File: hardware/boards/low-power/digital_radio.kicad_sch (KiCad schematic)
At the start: 34 parts, among them J1 U.FL, U1 SX1262IMLTRT, U2 SKY13453-385LF, Y1 32 MHz

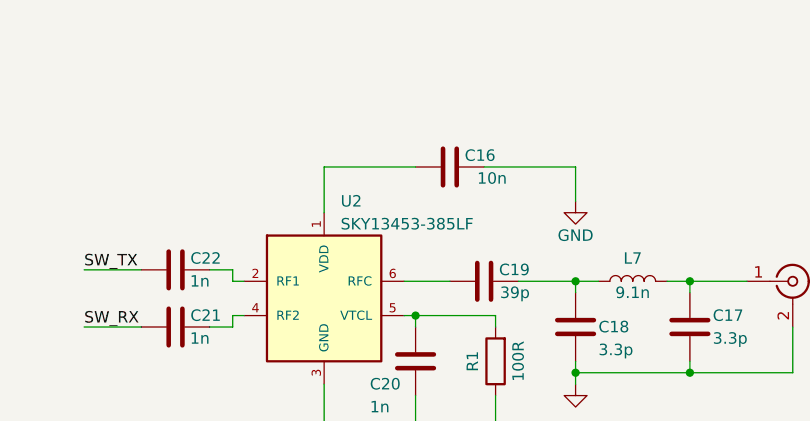
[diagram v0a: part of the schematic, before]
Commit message: fixup! Add low power PCB
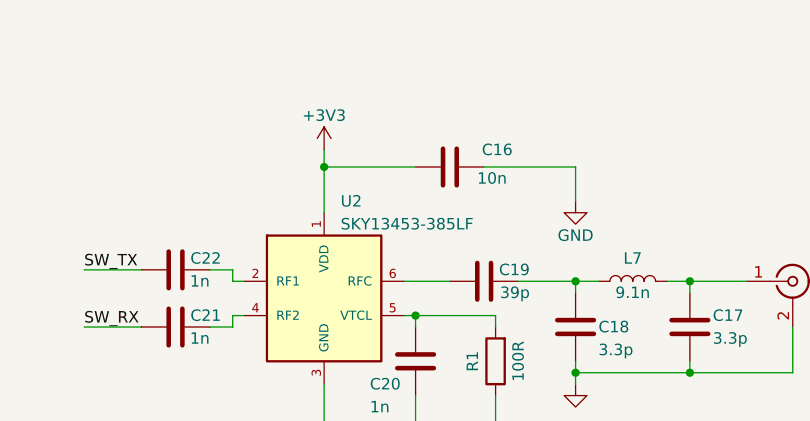
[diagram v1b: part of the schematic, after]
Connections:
- net +3V3: now also C16.1, U2.1 (VDD)
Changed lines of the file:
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@@
   (junction (at 112.395 102.235) (diameter 0) (color 0 0 0 0)
+  )
+  (junction (at 219.71 66.675) (diameter 0) (color 0 0 0 0)
   )
   (junction (at 139.065 79.375) (diameter 0) (color 0 0 0 0)
@@
   (no_connect (at 60.325 99.695))
   (wire (pts (xy 76.835 109.855) (xy 76.835 112.395))
+    (stroke (width 0) (type default))
+  )
+  (wire (pts (xy 219.71 64.77) (xy 219.71 66.675))
     (stroke (width 0) (type default))
   )
@@
   (symbol (lib_id "Device:C") (at 233.68 66.675 90) (unit 1)
     (in_bom yes) (on_board yes) (dnp no)
-    (property "Reference" "C16" (at 238.76 65.405 90)
+    (property "Reference" "C16" (at 240.665 64.77 90)
       (effects (font (size 1.27 1.27)) (justify left))
     )
@@
         )
       )
+    )
+  )
+  (symbol (lib_id "power:+3V3") (at 219.71 64.77 0) (unit 1)
+    (in_bom yes) (on_board yes) (dnp no) (fields_autoplaced)
+    (property "Reference" "#PWR0521" (at 219.71 68.58 0)
+      (effects (font (size 1.27 1.27)) hide)
+    )
+    (property "Value" "+3V3" (at 219.71 60.96 0)
+      (effects (font (size 1.27 1.27)))
+    )
+    (property "Footprint" "" (at 219.71 64.77 0)
+      (effects (font (size 1.27 1.27)) hide)
+    )
+    (property "Datasheet" "" (at 219.71 64.77 0)
+      (effects (font (size 1.27 1.27)) hide)
+    )
+    (pin "1")
+    (instances
+      (project "low-power"
+        (path "/71f6a5b4-1ac6-435b-9486-30b16ab86e62/9ba2378d-16cf-4aed-809c-215b19eeadaa"
+          (reference "#PWR0521") (unit 1)
+        )
+      )
